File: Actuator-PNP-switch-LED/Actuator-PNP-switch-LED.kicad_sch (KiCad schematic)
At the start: 6 parts, among them Q1 PNP

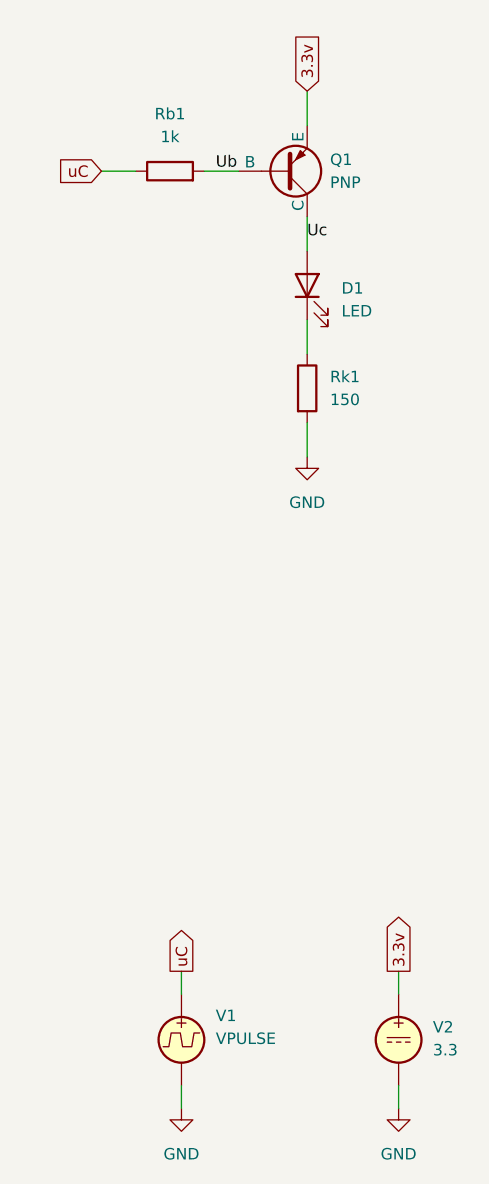
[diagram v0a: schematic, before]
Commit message: Tested/updated for KiCad 9
Schematics are tested and updated for KiCad 9, no changes in circuitry
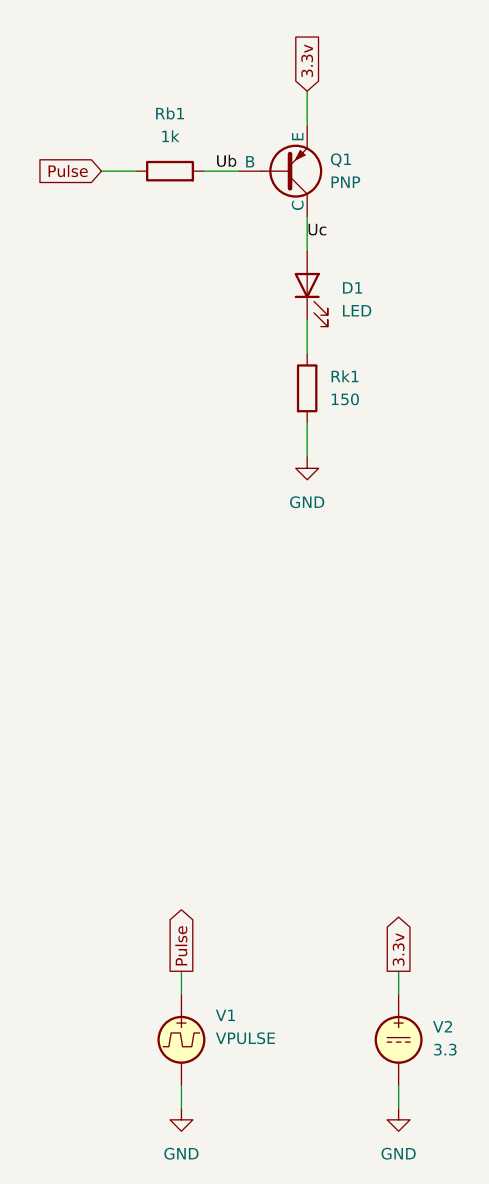
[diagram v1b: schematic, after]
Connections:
- net uC renamed Pulse
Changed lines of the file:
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@@
 (kicad_sch
-	(version 20231120)
+	(version 20250114)
 	(generator "eeschema")
-	(generator_version "8.0")
+	(generator_version "9.0")
 	(paper "A4")
 	(title_block
 		(title "PNP transistor as switch with LED")
-		(date "2024-12-15")
+		(date "2025-09-13")
 		(company "GitHub/OJStuff")
 	)
@@
 	(label "Ub"
 		(at 139.7 85.09 0)
-		(fields_autoplaced yes)
 		(effects
 			(font
@@
 	(label "Uc"
 		(at 149.86 92.71 0)
-		(fields_autoplaced yes)
 		(effects
 			(font
@@
 		)
 	)
-	(global_label "uC"
+	(global_label "Pulse"
 		(shape input)
 		(at 127 85.09 180)
@@
 		)
 		(property "Intersheetrefs" "${INTERSHEET_REFS}"
-			(at 121.5958 85.09 0)
+			(at 118.8139 85.09 0)
 			(effects
 				(font
@@
 		)
 	)
-	(global_label "uC"
+	(global_label "Pulse"
 		(shape output)
 		(at 135.89 173.99 90)
@@
 		)
 		(property "Intersheetrefs" "${INTERSHEET_REFS}"
-			(at 135.89 168.5858 90)
+			(at 135.89 165.8039 90)
 			(effects
 				(font
@@
 	)
 	(symbol
+		(lib_id "Device:LED")
+		(at 149.86 97.79 90)
+		(unit 1)
+		(exclude_from_sim no)
+		(in_bom yes)
+		(on_board yes)
+		(dnp no)
+		(fields_autoplaced yes)
+		(property "Reference" "D1"
+			(at 153.67 98.1074 90)
+			(effects
+				(font
+					(size 1.27 1.27)
+				)
+				(justify right)
+			)
+		)
+		(property "Value" "LED"
+			(at 153.67 100.6474 90)
+			(effects
+				(font
+					(size 1.27 1.27)
+				)
+				(justify right)
+			)
+		)
+		(property "Footprint" ""
+			(at 149.86 97.79 0)
+			(effects
+				(font
+					(size 1.27 1.27)
+				)
+				(hide yes)
+			)
+		)
+		(property "Datasheet" "~"
+			(at 149.86 97.79 0)
+			(effects
+				(font
+					(size 1.27 1.27)
+				)
+				(hide yes)
+			)
+		)
+		(property "Description" "Light emitting diode"
+			(at 149.86 97.79 0)
+			(effects
+				(font
+					(size 1.27 1.27)
+				)
+				(hide yes)
+			)
+		)
+		(property "Sim.Pins" "1=K 2=A"
+			(at 149.86 97.79 0)
+			(effects
+				(font
+					(size 1.27 1.27)
+				)
+				(hide yes)
+			)
+		)
+		(property "Sim.Library" "/home/ojs/Documents/GitHub/Schematics-Examples/Actuator-NPN-switch-LED/LED.lib"
+			(at 149.86 97.79 0)
+			(effects
+				(font
+					(size 1.27 1.27)
+				)
+				(hide yes)
+			)
+		)
+		(property "Sim.Name" "LED"
+			(at 149.86 97.79 0)
+			(effects
+				(font
+					(size 1.27 1.27)
+				)
+				(hide yes)
+			)
+		)
+		(property "Sim.Device" "D"
+			(at 149.86 97.79 0)
+			(effects
+				(font
+					(size 1.27 1.27)
+				)
+				(hide yes)
+			)
+		)
+		(pin "1"
+		)
+		(pin "2"
+		)
+		(instances
+			(project ""
+				(path "/5efcba29-6960-4983-8205-1ea3cd09c91f"
+					(reference "D1")
+					(unit 1)
+				)
+			)
+		)
+	)
+	(symbol
 		(lib_id "Device:R")
 		(at 134.62 85.09 90)
@@
 	)
 	(symbol
-		(lib_id "Device:LED")
-		(at 149.86 97.79 90)
-		(unit 1)
-		(exclude_from_sim no)
-		(in_bom yes)
-		(on_board yes)
-		(dnp no)
-		(fields_autoplaced yes)
-		(property "Reference" "D1"
-			(at 153.67 98.1074 90)
-			(effects
-				(font
-					(size 1.27 1.27)
-				)
-				(justify right)
-			)
-		)
-		(property "Value" "LED"
-			(at 153.67 100.6474 90)
-			(effects
-				(font
-					(size 1.27 1.27)
-				)
-				(justify right)
-			)
-		)
-		(property "Footprint" ""
-			(at 149.86 97.79 0)
-			(effects
-				(font
-					(size 1.27 1.27)
-				)
-				(hide yes)
-			)
-		)
-		(property "Datasheet" "~"
-			(at 149.86 97.79 0)
-			(effects
-				(font
-					(size 1.27 1.27)
-				)
-				(hide yes)
-			)
-		)
-		(property "Description" "Light emitting diode"
-			(at 149.86 97.79 0)
-			(effects
-				(font
-					(size 1.27 1.27)
-				)
-				(hide yes)
-			)
-		)
-		(property "Sim.Device" "D"
-			(at 149.86 97.79 0)
-			(effects
-				(font
-					(size 1.27 1.27)
-				)
-				(hide yes)
-			)
-		)
-		(property "Sim.Pins" "1=K 2=A"
-			(at 149.86 97.79 0)
-			(effects
-				(font
-					(size 1.27 1.27)
-				)
-				(hide yes)
-			)
-		)
-		(property "Sim.Library" "LED.lib"
-			(at 149.86 97.79 0)
-			(effects
-				(font
-					(size 1.27 1.27)
-				)
-				(hide yes)
-			)
-		)
-		(property "Sim.Name" "LED"
-			(at 149.86 97.79 0)
-			(effects
-				(font
-					(size 1.27 1.27)
-				)
-				(hide yes)
-			)
-		)
-		(pin "2"
-		)
-		(pin "1"
-		)
-		(instances
-			(project ""
-				(path "/5efcba29-6960-4983-8205-1ea3cd09c91f"
-					(reference "D1")
-					(unit 1)
-				)
-			)
-		)
-	)
-	(symbol
 		(lib_id "power:GND")
 		(at 149.86 116.84 0)
@@
 		)
 	)
+	(embedded_fonts no)
 )
